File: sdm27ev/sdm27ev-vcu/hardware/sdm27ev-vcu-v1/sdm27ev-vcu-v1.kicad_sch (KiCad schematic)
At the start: 30 parts, among them J1 6437288-1, J2 6437288-1, J4 2201778-1, SW1 SW_Push, SW2 SW_Push, SW3 SW_Push, U1 ESP32-P4-Core, U2 CH32V003JxMx

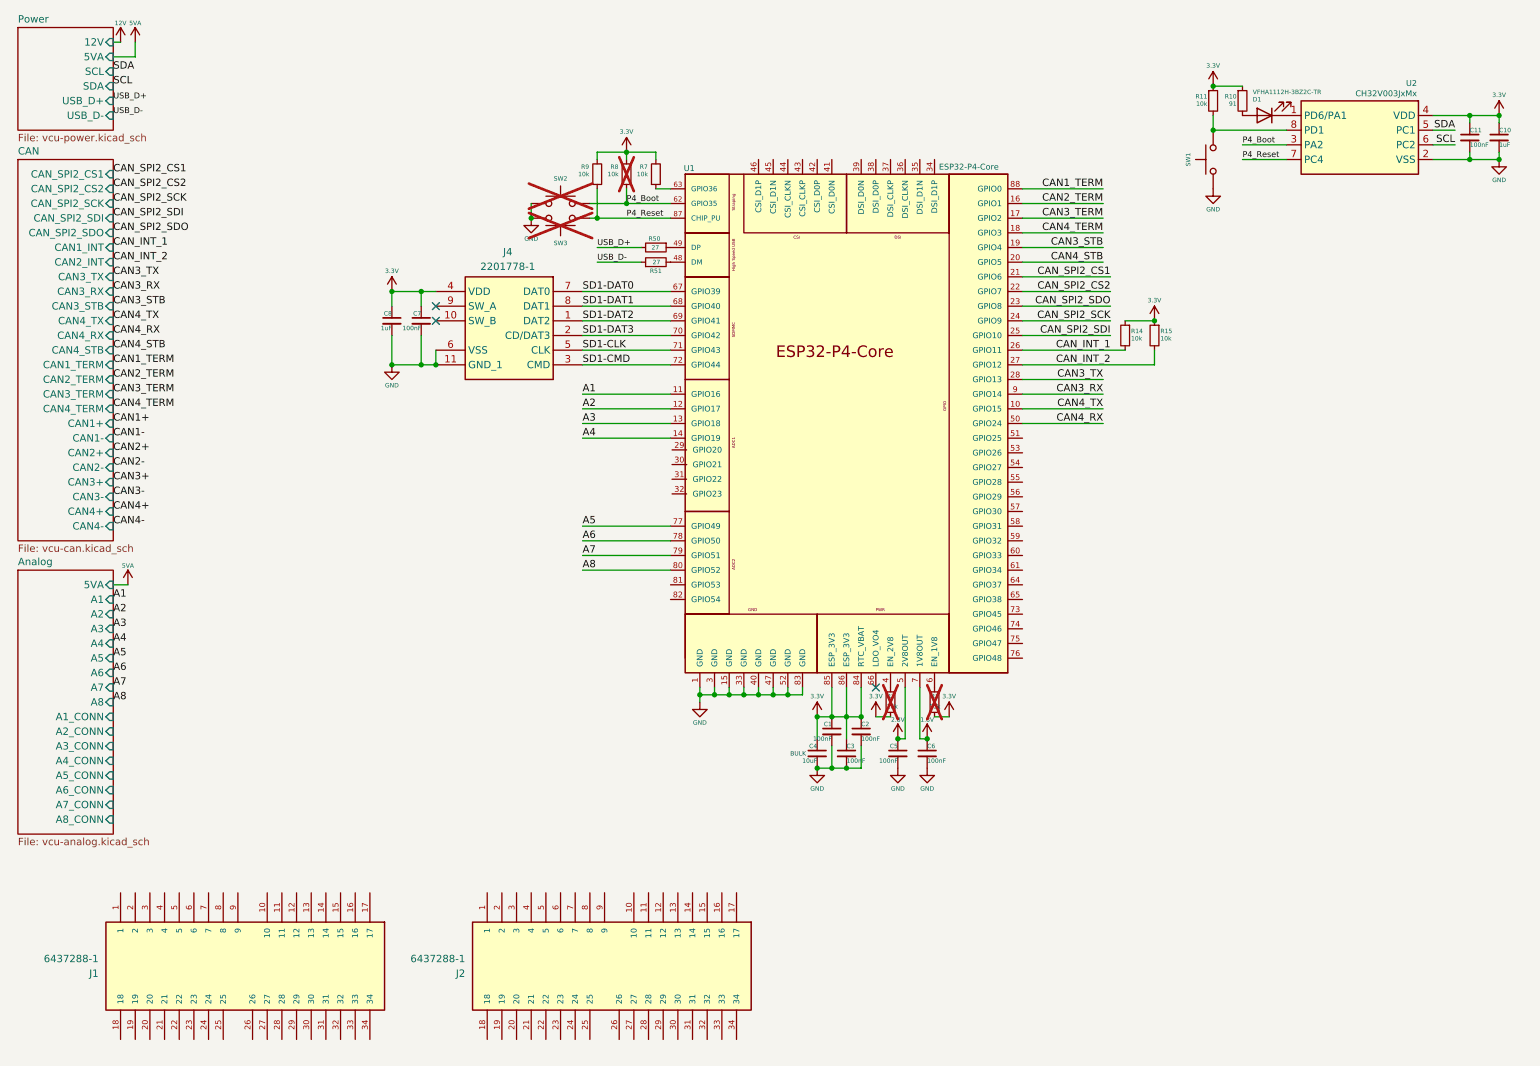
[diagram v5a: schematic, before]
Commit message: EV27 VCU, analog front end. still needs analog power protection
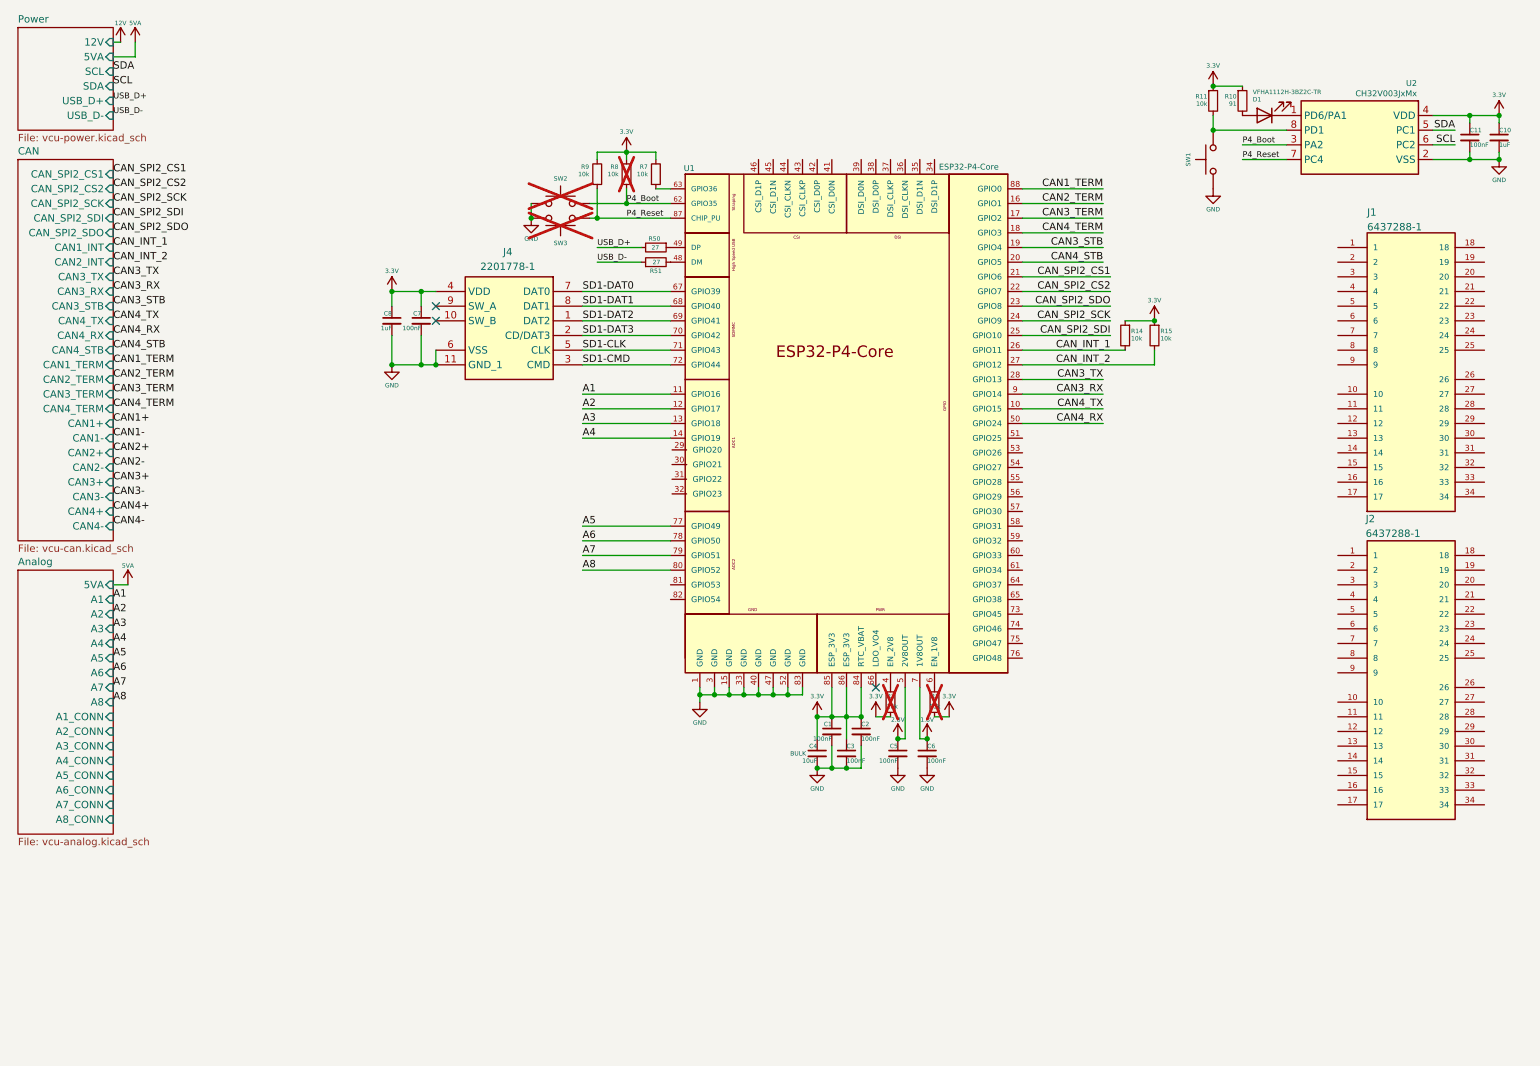
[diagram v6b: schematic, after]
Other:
- moved on the sheet: J1, J2
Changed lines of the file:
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@@
 	(symbol
 		(lib_id "EV VCU:6437288-1")
-		(at 116.84 177.8 90)
-		(mirror x)
+		(at 254 129.54 0)
 		(unit 1)
 		(body_style 1)
@@
 		(dnp no)
 		(property "Reference" "J2"
-			(at 90.17 179.0701 90)
+			(at 246.126 100.33 0)
 			(show_name no)
 			(do_not_autoplace no)
@@
 		)
 		(property "Value" "6437288-1"
-			(at 90.17 176.5301 90)
+			(at 246.126 102.87 0)
 			(show_name no)
 			(do_not_autoplace no)
@@
 		)
 		(property "Footprint" "SDM27 EV VCU:TE_6437288-1"
-			(at 116.84 177.8 0)
+			(at 254 129.54 0)
 			(hide yes)
 			(show_name no)
@@
 		)
 		(property "Datasheet" ""
-			(at 116.84 177.8 0)
+			(at 254 129.54 0)
 			(hide yes)
 			(show_name no)
@@
 		)
 		(property "Description" "34 Position 4 Row Right Angle Receptacle Through Hole Super Seal Cap Assy"
-			(at 116.84 177.8 0)
+			(at 254 129.54 0)
 			(hide yes)
 			(show_name no)
@@
 		)
 		(property "COMMENT" "6437288-1"
-			(at 116.84 177.8 0)
+			(at 254 129.54 0)
 			(hide yes)
 			(show_name no)
@@
 		)
 		(property "MF" "TE Connectivity"
-			(at 116.84 177.8 0)
+			(at 254 129.54 0)
 			(hide yes)
 			(show_name no)
@@
 		)
 		(property "PACKAGE" "None"
-			(at 116.84 177.8 0)
+			(at 254 129.54 0)
 			(hide yes)
 			(show_name no)
@@
 		)
 		(property "PRICE" "None"
-			(at 116.84 177.8 0)
+			(at 254 129.54 0)
 			(hide yes)
 			(show_name no)
@@
 		)
 		(property "TE_PURCHASE_URL" "https://www.te.com/usa-en/product-6437288-1.html?te_bu=Cor&te_type=disp&te_campaign=seda_glo_cor-seda-global-disp-prtnr-fy19-seda-model-bom-cta_sma-317_1&elqCampaignId=32493"
-			(at 116.84 177.8 0)
+			(at 254 129.54 0)
 			(hide yes)
 			(show_name no)
@@
 		)
 		(property "STANDARD" "Manufacturer Recommended"
-			(at 116.84 177.8 0)
+			(at 254 129.54 0)
 			(hide yes)
 			(show_name no)
@@
 		)
 		(property "PARTREV" "A1"
-			(at 116.84 177.8 0)
+			(at 254 129.54 0)
 			(hide yes)
 			(show_name no)
@@
 		)
 		(property "MP" "6437288-1"
-			(at 116.84 177.8 0)
+			(at 254 129.54 0)
 			(hide yes)
 			(show_name no)
@@
 		)
 		(property "EU_ROHS_COMPLIANCE" "Compliant"
-			(at 116.84 177.8 0)
+			(at 254 129.54 0)
 			(hide yes)
 			(show_name no)
@@
 		)
 		(property "AVAILABILITY" "Unavailable"
-			(at 116.84 177.8 0)
+			(at 254 129.54 0)
 			(hide yes)
 			(show_name no)
@@
 	(symbol
 		(lib_id "EV VCU:6437288-1")
-		(at 53.34 177.8 90)
-		(mirror x)
+		(at 254 76.2 0)
 		(unit 1)
 		(body_style 1)
@@
 		(dnp no)
 		(property "Reference" "J1"
-			(at 26.67 179.0701 90)
+			(at 246.38 47.244 0)
 			(show_name no)
 			(do_not_autoplace no)
@@
 		)
 		(property "Value" "6437288-1"
-			(at 26.67 176.5301 90)
+			(at 246.38 49.784 0)
 			(show_name no)
 			(do_not_autoplace no)
@@
 		)
 		(property "Footprint" "SDM27 EV VCU:TE_6437288-1"
-			(at 53.34 177.8 0)
+			(at 254 76.2 0)
 			(hide yes)
 			(show_name no)
@@
 		)
 		(property "Datasheet" ""
-			(at 53.34 177.8 0)
+			(at 254 76.2 0)
 			(hide yes)
 			(show_name no)
@@
 		)
 		(property "Description" "34 Position 4 Row Right Angle Receptacle Through Hole Super Seal Cap Assy"
-			(at 53.34 177.8 0)
+			(at 254 76.2 0)
 			(hide yes)
 			(show_name no)
@@
 		)
 		(property "COMMENT" "6437288-1"
-			(at 53.34 177.8 0)
+			(at 254 76.2 0)
 			(hide yes)
 			(show_name no)
@@
 		)
 		(property "MF" "TE Connectivity"
-			(at 53.34 177.8 0)
+			(at 254 76.2 0)
 			(hide yes)
 			(show_name no)
@@
 		)
 		(property "PACKAGE" "None"
-			(at 53.34 177.8 0)
+			(at 254 76.2 0)
 			(hide yes)
 			(show_name no)
@@
 		)
 		(property "PRICE" "None"
-			(at 53.34 177.8 0)
+			(at 254 76.2 0)
 			(hide yes)
 			(show_name no)
@@
 		)
 		(property "TE_PURCHASE_URL" "https://www.te.com/usa-en/product-6437288-1.html?te_bu=Cor&te_type=disp&te_campaign=seda_glo_cor-seda-global-disp-prtnr-fy19-seda-model-bom-cta_sma-317_1&elqCampaignId=32493"
-			(at 53.34 177.8 0)
+			(at 254 76.2 0)
 			(hide yes)
 			(show_name no)
@@
 		)
 		(property "STANDARD" "Manufacturer Recommended"
-			(at 53.34 177.8 0)
+			(at 254 76.2 0)
 			(hide yes)
 			(show_name no)
@@
 		)
 		(property "PARTREV" "A1"
-			(at 53.34 177.8 0)
+			(at 254 76.2 0)
 			(hide yes)
 			(show_name no)
@@
 		)
 		(property "MP" "6437288-1"
-			(at 53.34 177.8 0)
+			(at 254 76.2 0)
 			(hide yes)
 			(show_name no)
@@
 		)
 		(property "EU_ROHS_COMPLIANCE" "Compliant"
-			(at 53.34 177.8 0)
+			(at 254 76.2 0)
 			(hide yes)
 			(show_name no)
@@
 		)
 		(property "AVAILABILITY" "Unavailable"
-			(at 53.34 177.8 0)
-			(hide yes)
-			(show_name no)
+			(at 254 76.2 0)
+			(hide yes)
+			(show_name no)
